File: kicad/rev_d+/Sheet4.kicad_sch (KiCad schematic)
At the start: 28 parts, among them J2 JUMPER, J3 JUMPER, X26 ext. video/sound, X7 DB15VGA, X8 PLB1-4I, X9 PLB1-2

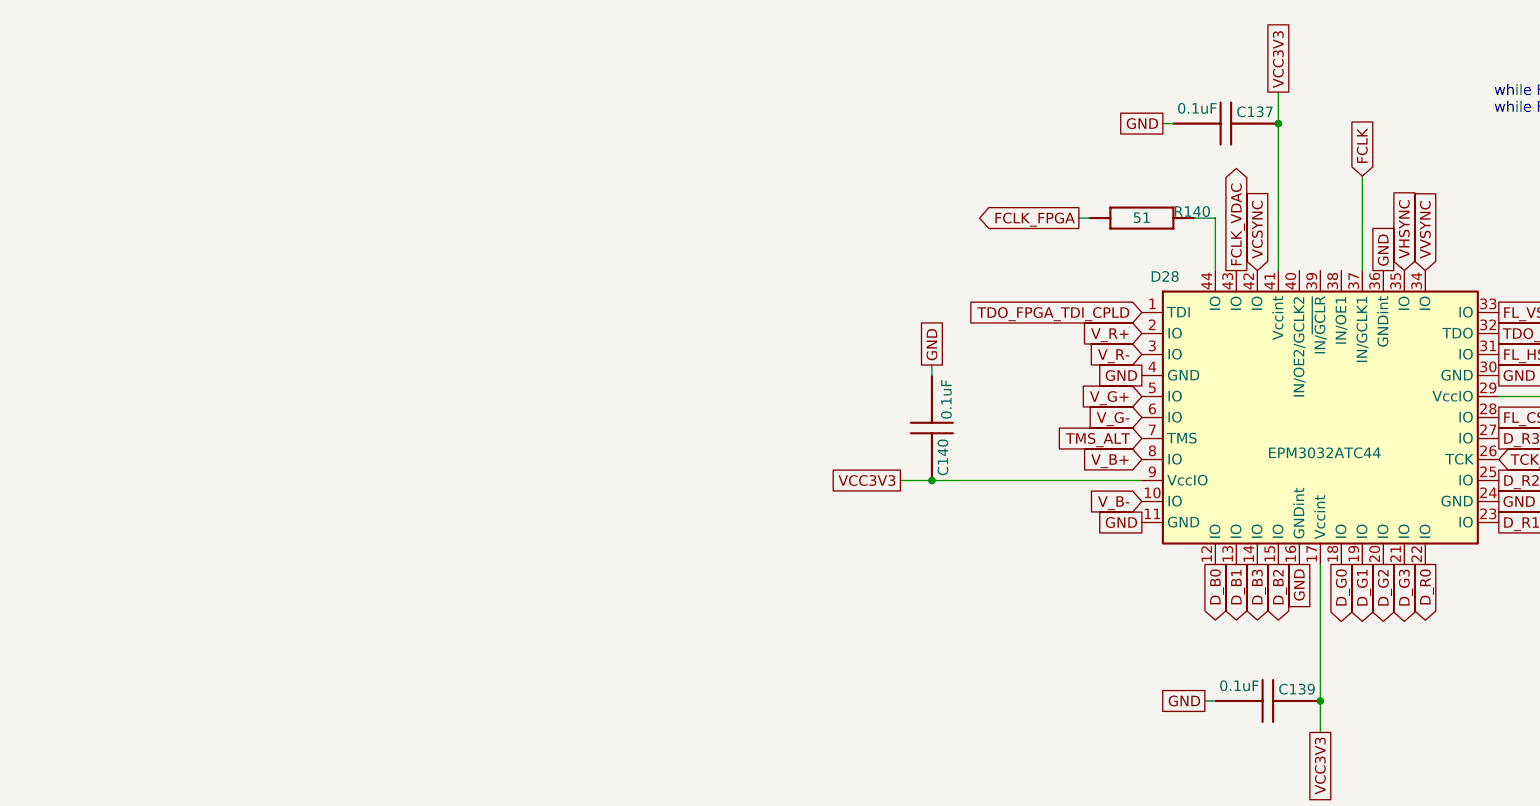
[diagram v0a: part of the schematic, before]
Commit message: pentevo: rev D+: add option to have EPM3032 in PLCC
git-svn-id: svn://localhost/local-pentevo@1343 c6c76956-fad2-4150-a3a9-ea0a427205ba
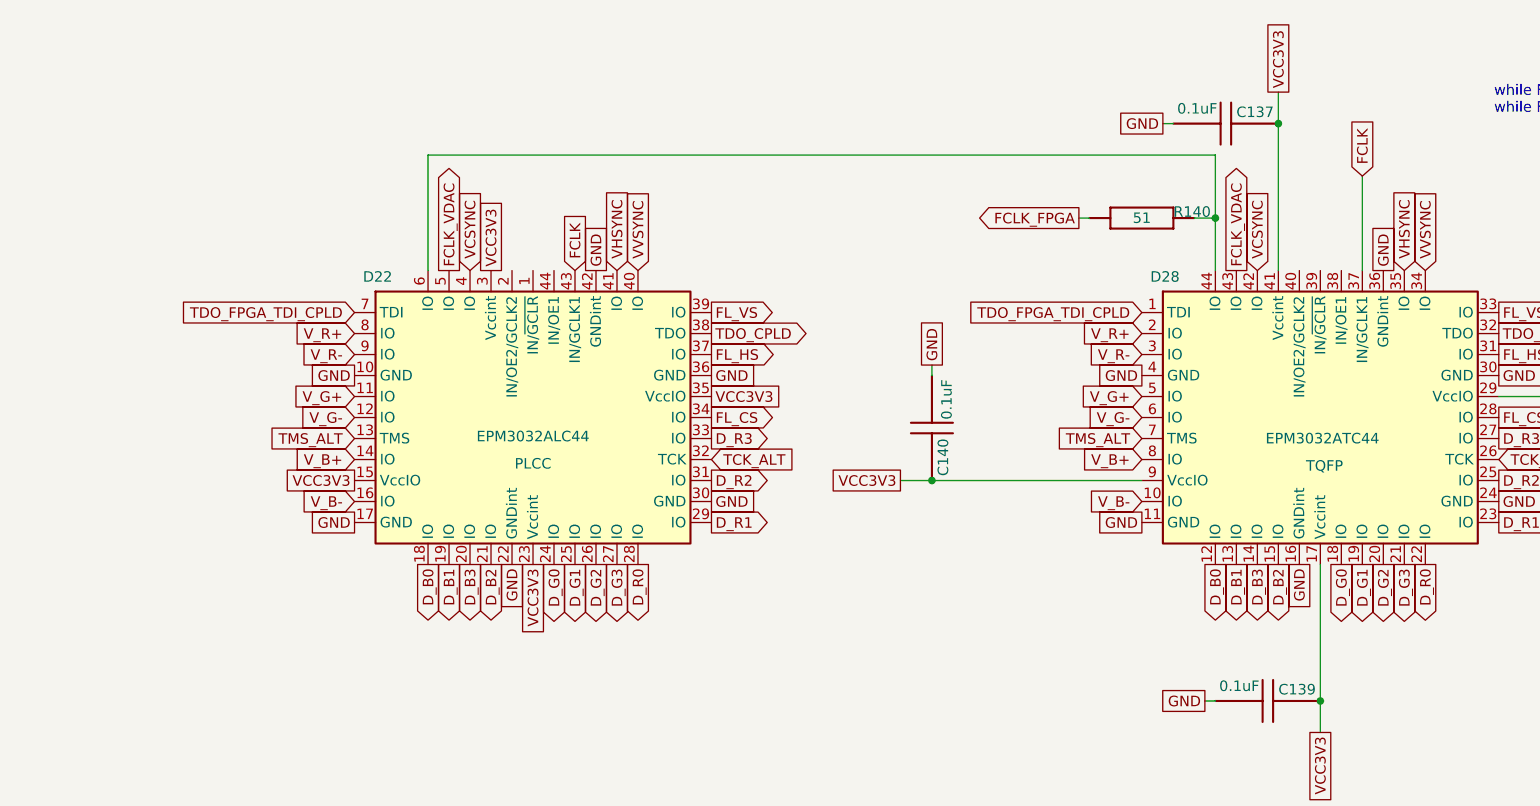
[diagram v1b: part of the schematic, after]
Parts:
- added D22: EPM3032ALC44, symbol eva-altium-import:EPM3032ATC44
- D28: footprint (none) -> Package_QFP:TQFP-44_10x10mm_P0.8mm
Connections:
- net D_B0: now also D22.18 (IO)
- net D_B1: now also D22.19 (IO)
- net D_B2: now also D22.21 (IO)
- net D_B3: now also D22.20 (IO)
- net D_G0: now also D22.24 (IO)
- net D_G1: now also D22.25 (IO)
- net D_G2: now also D22.26 (IO)
- net D_G3: now also D22.27 (IO)
- net D_R0: now also D22.28 (IO)
- net D_R1: now also D22.29 (IO)
- net D_R2: now also D22.31 (IO)
- net D_R3: now also D22.33 (IO)
- net FCLK: now also D22.43 (IN/GCLK1)
- net FCLK_VDAC: now also D22.5 (IO)
- net FL_CS: now also D22.34 (IO)
- net FL_HS: now also D22.37 (IO)
- net FL_VS: now also D22.39 (IO)
- net GND: now also D22.10 (GND), D22.17 (GND), D22.22 (GNDint), D22.30 (GND), D22.36 (GND), D22.42 (GNDint)
- net TCK_ALT: now also D22.32 (TCK)
- net TDO_CPLD: now also D22.38 (TDO)
- net TDO_FPGA_TDI_CPLD: now also D22.7 (TDI)
- net TMS_ALT: now also D22.13 (TMS)
- net VCC3V3: now also D22.15 (VccIO), D22.23 (Vccint), D22.3 (Vccint), D22.35 (VccIO)
- net VCSYNC: now also D22.4 (IO)
- net VHSYNC: now also D22.41 (IO)
- net VVSYNC: now also D22.40 (IO)
- net V_B+: now also D22.14 (IO)
- net V_B-: now also D22.16 (IO)
- net V_G+: now also D22.11 (IO)
- net V_G-: now also D22.12 (IO)
- net V_R+: now also D22.8 (IO)
- net V_R-: now also D22.9 (IO)
- net at D28.44 (IO), R140.2 (i/o1): now also D22.6 (IO)

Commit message: pentevo: rev D+: add option to have TDA8772
git-svn-id: svn://localhost/local-pentevo@1345 c6c76956-fad2-4150-a3a9-ea0a427205ba
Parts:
- added C155, C156, C157, C158, C159: 10nF, C-CHIP, symbol eva-altium-import:Sheet1_0_CAPCHIP
- added C160: 0.1uF, C-CHIP, symbol eva-altium-import:Sheet1_0_CAPCHIP
- added D23: TDA8772, symbol Video:TDA8772
- added R220: 8k2, R-CHIP, symbol eva-altium-import:Sheet1_0_RESCHIP
- added R223: 33k, R-CHIP, symbol eva-altium-import:Sheet1_0_RESCHIP
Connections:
- net D_B0: now also D23.27 (B4), D23.31 (B0)
- net D_B1: now also D23.26 (B5), D23.30 (B1)
- net D_B2: now also D23.25 (B6), D23.29 (B2)
- net D_B3: now also D23.24 (B7), D23.28 (B3)
- net D_G0: now also D23.16 (G4), D23.20 (G0)
- net D_G1: now also D23.15 (G5), D23.19 (G1)
- net D_G2: now also D23.14 (G6), D23.18 (G2)
- net D_G3: now also D23.13 (G7), D23.17 (G3)
- net D_R0: now also D23.4 (R4), D23.8 (R0)
- net D_R1: now also D23.3 (R5), D23.7 (R1)
- net D_R2: now also D23.2 (R6), D23.6 (R2)
- net D_R3: now also D23.1 (R7), D23.5 (R3)
- net FCLK_VDAC: now also D23.21 (CLKR), D23.22 (CLKG), D23.23 (CLKB)
- net GND: now also C155.2, C156.2, C157.2, C158.2, C159.2, C160.2, D23.11 (SYNC), D23.33 (GND), D23.37 (GNDA), D23.42 (GNDA), D23.9 (GND), R223.1 (i/o)
- net OUT_B: now also D23.36 (BLU)
- net OUT_G: now also D23.40 (GRE)
- net OUT_R: now also D23.44 (RED)
- net VIDEOVCC: now also C155.1, C156.1, C157.1, C158.1, C159.1, D23.10 (VCC), D23.12 (BLANK), D23.32 (VCC), D23.35 (VCCA), D23.39 (VCCA), D23.43 (VCCA), R220.1 (i/o)
- new net: D23.41 (IRFB), R220.2 (i/o1)
- new net: D23.38 (IRFA), R223.2 (i/o1)
- new net: C160.1, D23.34 (VRD)
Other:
- note added: "place either ADV7125 or TDA8772"
- moved on the sheet: C137, C138, C139, C140, C73, C74, C76, D22, D28, L3, R127, R140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
